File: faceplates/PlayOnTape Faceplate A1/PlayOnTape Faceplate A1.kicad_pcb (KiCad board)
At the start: 2 copper layers, 99.7 x 64.1 mm, 15 parts, among them IC1 0.96_I2C_OLED, J1 I2C_VOL, J2 SPI, J3 EXTENSION, M1 Mounting, M2 Mounting, M3 Mounting, M4 Mounting

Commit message: Reroute some tracks
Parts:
- moved JP1 2.54 mm to (160.0, 95.2), turned to 90 degrees
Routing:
- net GND: track 19.8 -> 12.1 mm, vias 4 -> 1
- net Net-(IC1-Pad1): track 46.6 -> 51.4 mm
- net VCC: track 31.9 -> 34.6 mm
- net Net-(IC1-Pad2): track 45.7 -> 44.0 mm

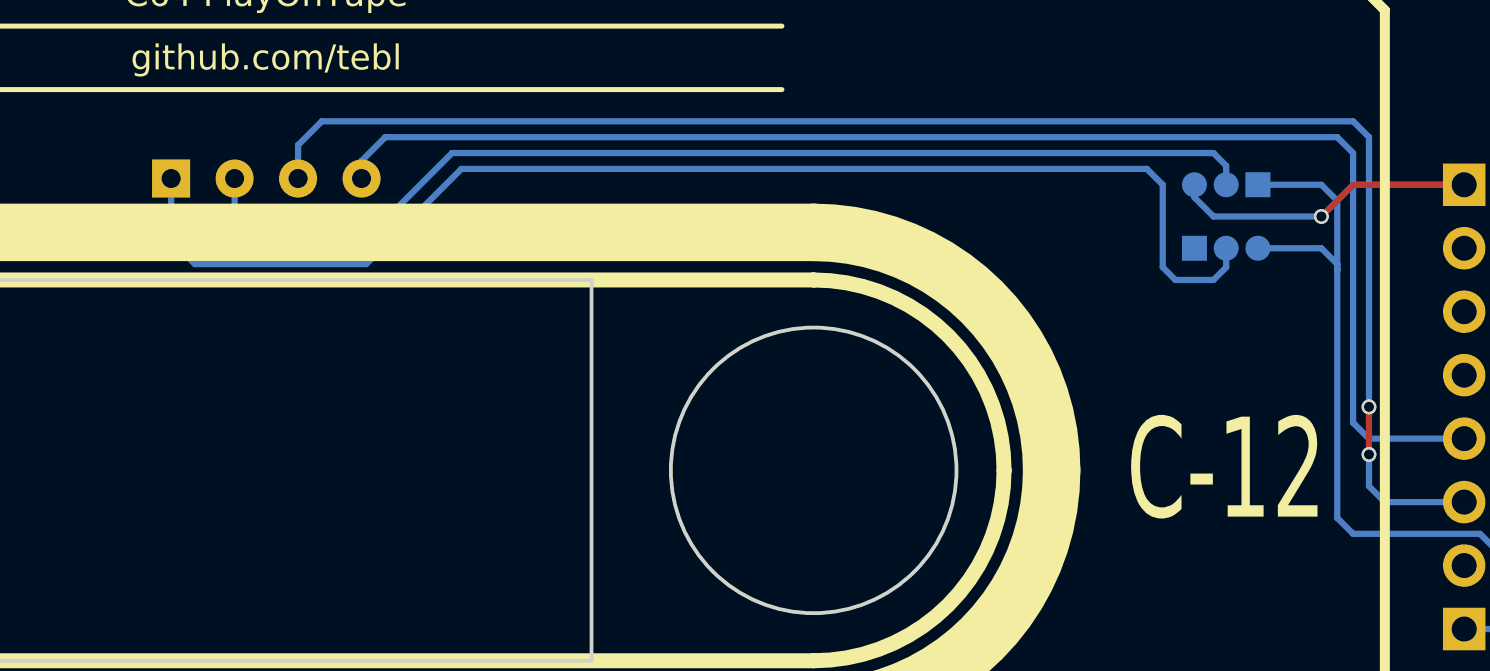
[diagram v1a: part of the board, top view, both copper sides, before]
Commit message: Fixed OLED jumpers
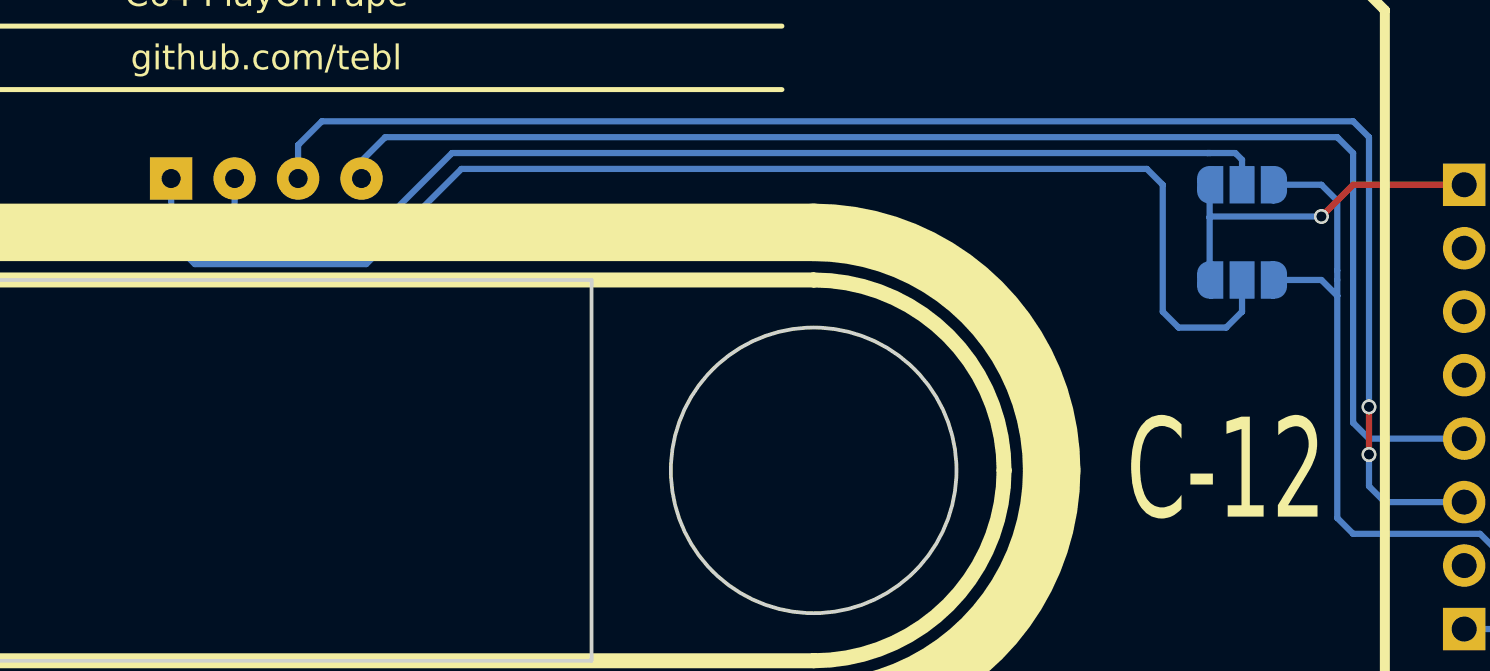
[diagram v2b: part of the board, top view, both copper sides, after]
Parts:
- JP1, JP2: footprint wire_pads:OLED_SEL -> Jumper:SolderJumper-3_P1.3mm_Open_RoundedPad1.0x1.5mm
- moved JP2 2.29 mm to (159.4, 99.1), turned to 0 degrees
- moved JP1 0.64 mm to (159.4, 95.2), turned to 180 degrees
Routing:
- net Net-(IC1-Pad1): track 51.4 -> 54.4 mm
- net GND: track 12.1 -> 14.5 mm
- net VCC: track 34.6 -> 33.0 mm
- net Net-(IC1-Pad2): track 44.0 -> 44.7 mm

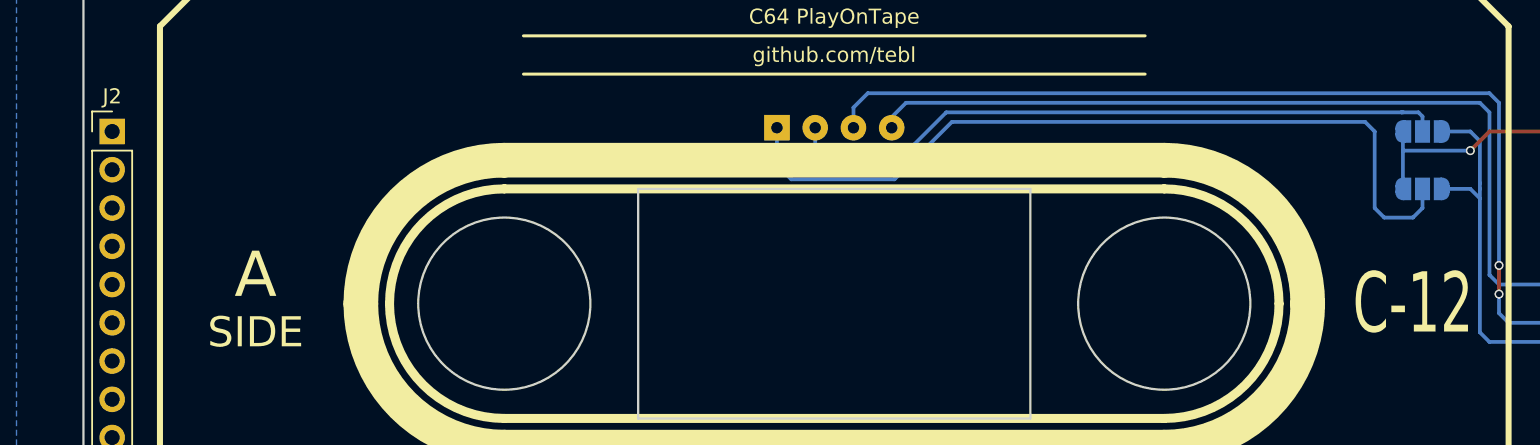
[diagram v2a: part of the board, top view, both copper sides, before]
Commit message: Changed to use IDC cable
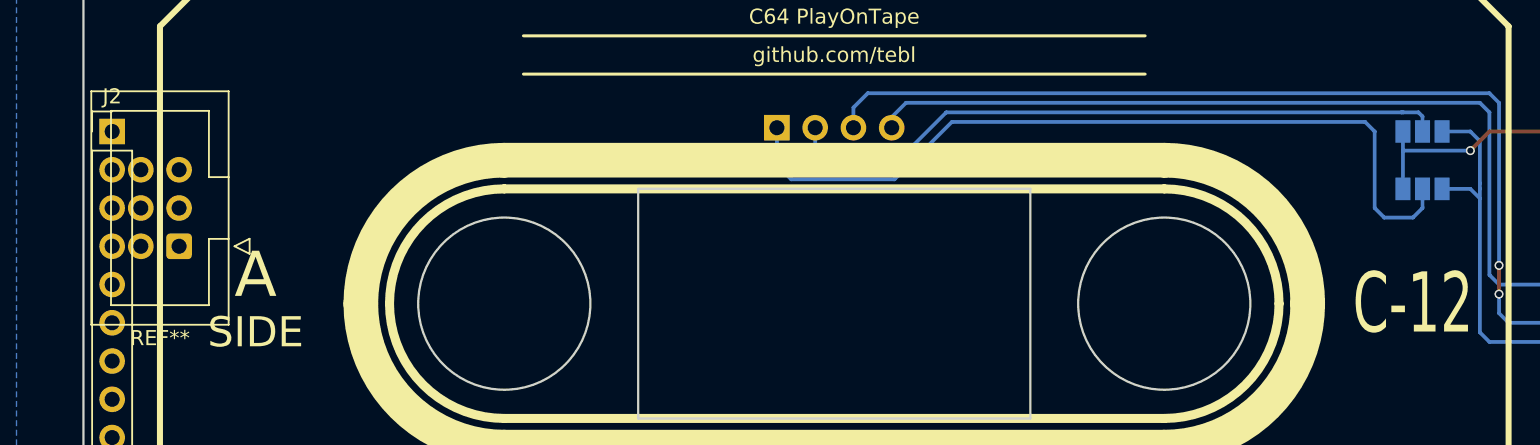
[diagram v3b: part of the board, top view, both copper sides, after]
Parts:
- added REF**: IDC-Header_2x03_P2.54mm_Vertical, Connector_IDC:IDC-Header_2x03_P2.54mm_Vertical, F.Cu at (76.8, 102.9)
- JP1, JP2: footprint Jumper:SolderJumper-3_P1.3mm_Open_RoundedPad1.0x1.5mm -> Jumper:SolderJumper-3_P1.3mm_Open_Pad1.0x1.5mm

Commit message: Add connector cutout
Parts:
- removed J2: SPI, Pin_Headers:Pin_Header_Straight_1x10_Pitch2.54mm
- removed the REF** at (76.8, 102.9)
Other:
- outline, holes or cut-outs redrawn
- board text removed: "SIDE"
